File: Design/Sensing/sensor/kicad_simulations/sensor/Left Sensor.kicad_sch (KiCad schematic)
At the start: 9 parts, among them Q3 2N3904, U3 TSSP58038

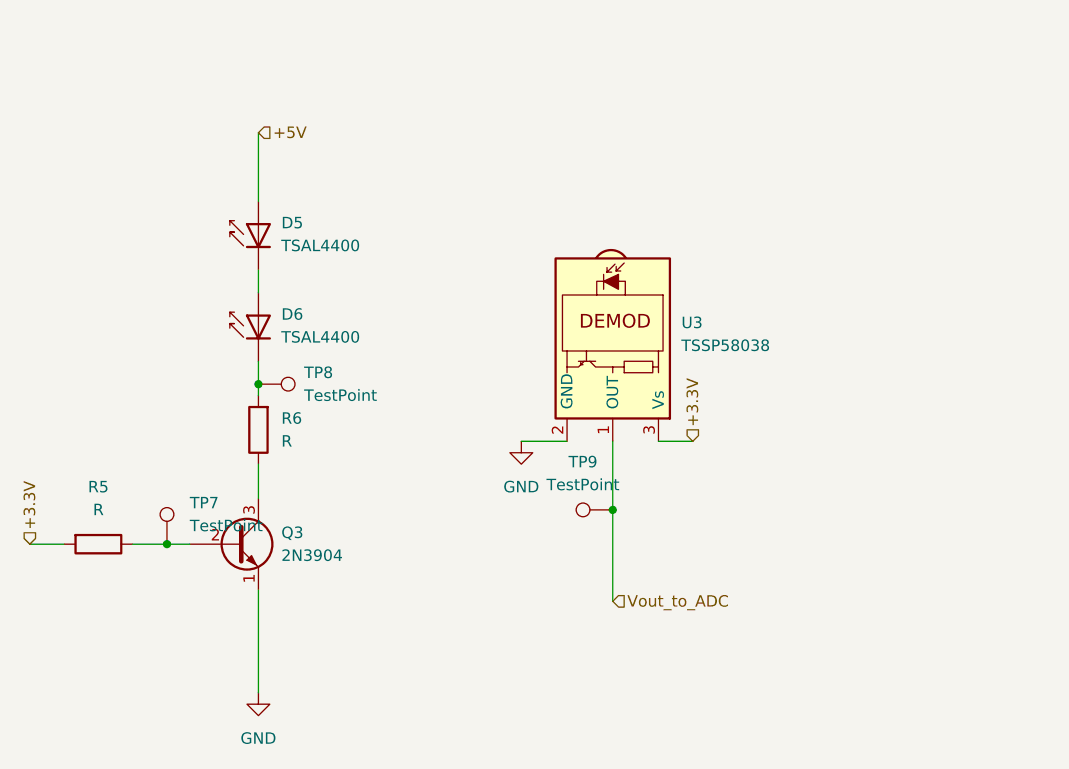
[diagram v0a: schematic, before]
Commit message: Resistor values for emitter circuit done, still have to name the circuits properly
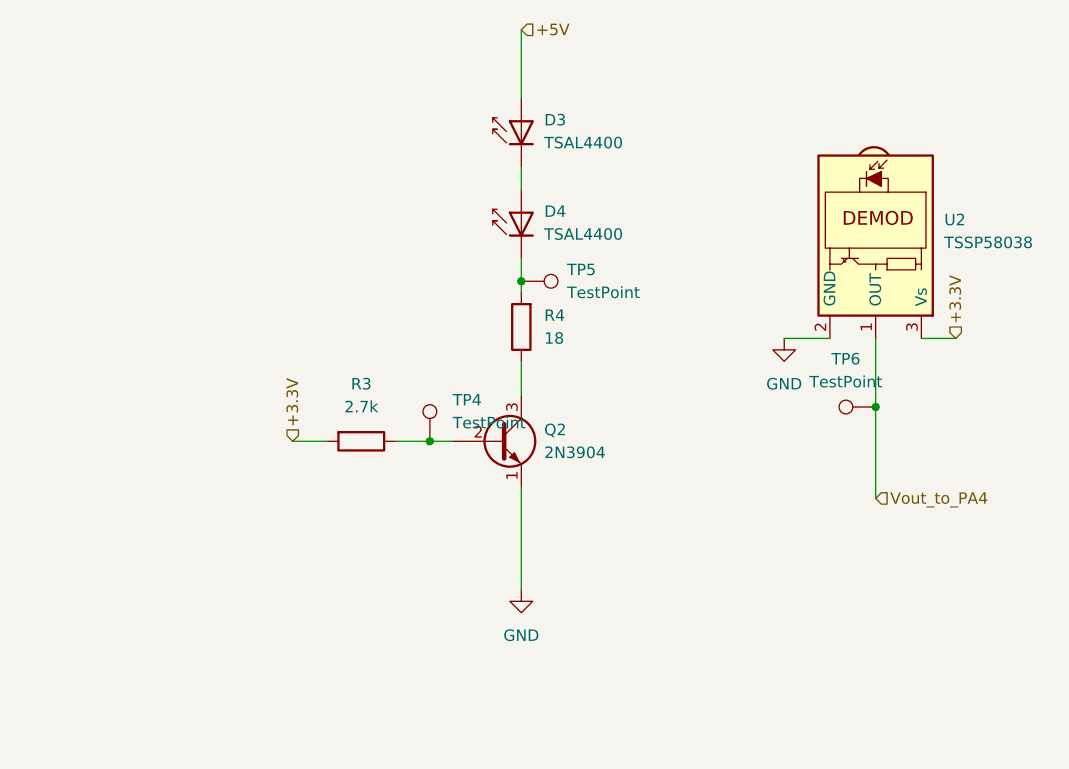
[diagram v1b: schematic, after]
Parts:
- removed D5, D6: TSAL4400, LED_THT:LED_D3.0mm_IRBlack, symbol LED:TSAL4400
- removed Q3: 2N3904, Package_TO_SOT_THT:TO-92_Inline, symbol Transistor_BJT:2N3904
- removed R5, R6: R, symbol Device:R
- removed TP7, TP8, TP9: TestPoint, symbol Connector:TestPoint
- removed U3: TSSP58038, OptoDevice:Vishay_MINICAST-3Pin, symbol Sensor_Proximity:TSSP58038
- added D3, D4: TSAL4400, LED_THT:LED_D3.0mm_IRBlack, symbol LED:TSAL4400
- added Q2: 2N3904, Package_TO_SOT_THT:TO-92_Inline, symbol Transistor_BJT:2N3904
- added R3: 2.7k, symbol Device:R
- added R4: 18, symbol Device:R
- added TP4, TP5, TP6: TestPoint, symbol Connector:TestPoint
- added U2: TSSP58038, OptoDevice:Vishay_MINICAST-3Pin, symbol Sensor_Proximity:TSSP58038
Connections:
- net +3.3V: now also R3.2, U2.3 (Vs)
- net +5V: now also D3.2 (A)
- net GND: now also Q2.1 (E), U2.2 (GND)
- new net: Q2.3 (C), R4.1
- new net: D4.1 (K), R4.2, TP5.1
- new net: D3.1 (K), D4.2 (A)
- new net: Q2.2 (B), R3.1, TP4.1
- new net Vout_to_PA4: TP6.1, U2.1 (OUT)
